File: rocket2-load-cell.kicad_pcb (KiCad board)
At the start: 2 copper layers, 69 x 67 mm, 38 parts, among them J1 SWD, J2 Screw_Terminal_01x02, U2 STM32F103C8Tx, U3 AMS1117-3.3, Y1 16MHz

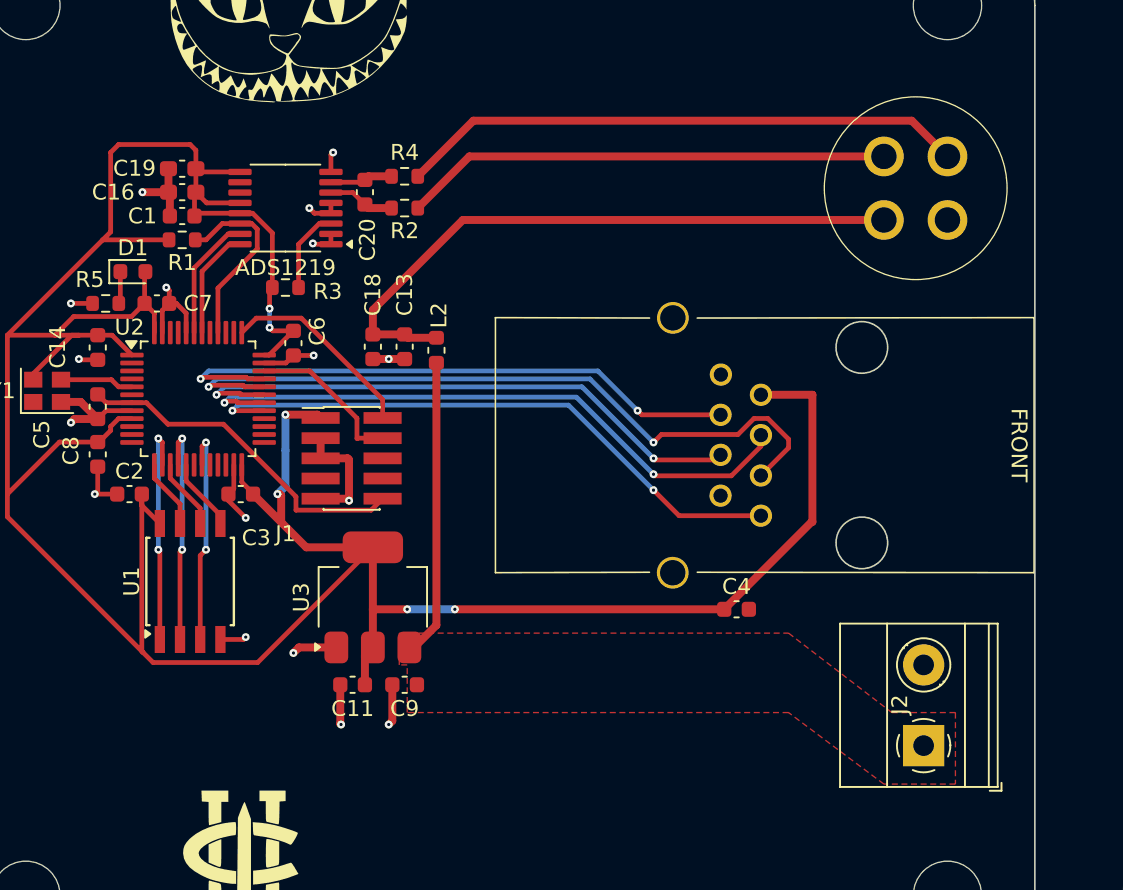
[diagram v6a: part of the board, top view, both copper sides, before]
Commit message: added gx12 connector and fixed varioius other design problems
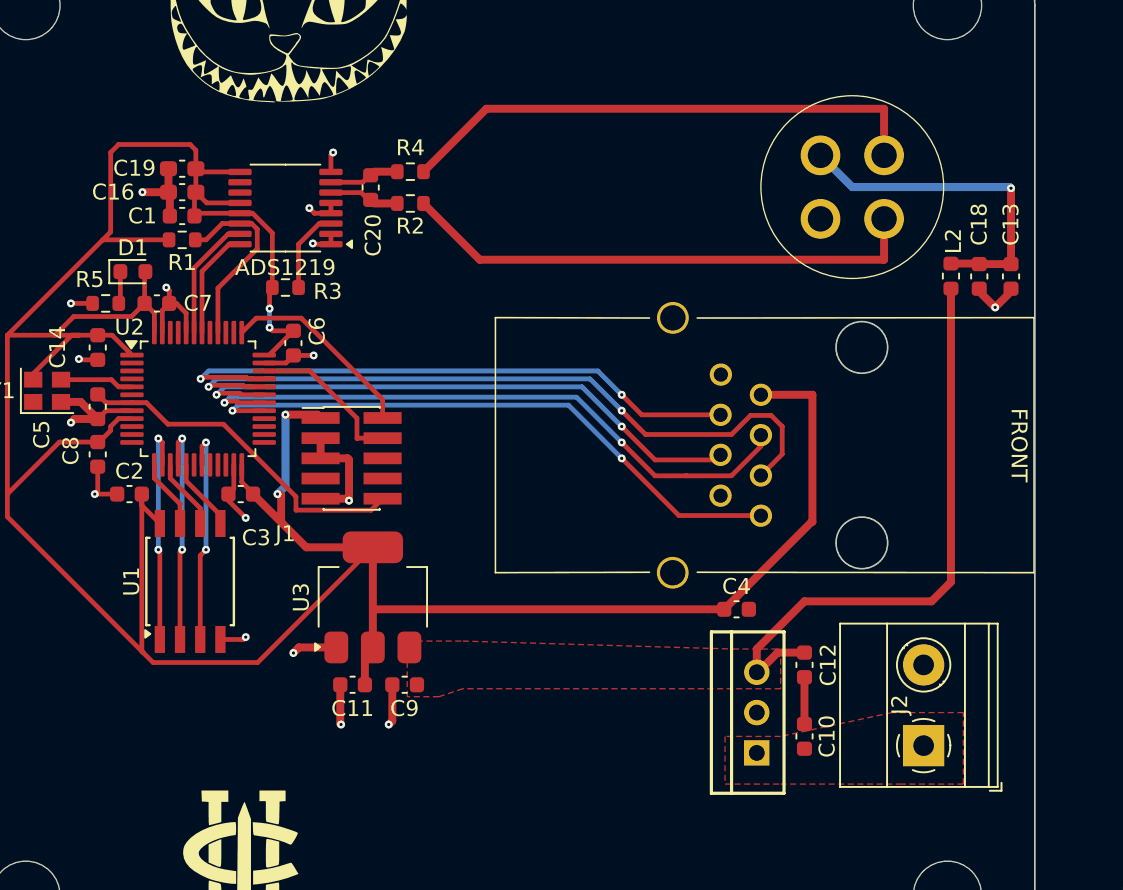
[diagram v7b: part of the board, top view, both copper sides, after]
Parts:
- added C10: .33uF, Capacitor_SMD:C_0603_1608Metric, F.Cu at (175.0, 133.5)
- added C12: .1uF, Capacitor_SMD:C_0603_1608Metric, F.Cu at (175.0, 129.0)
- added U4: UA7812CKCS, ucirp:KCS0003B, F.Cu at (172.0, 132.0)
- moved C13 38.4 mm to (188.0, 104.5)
- moved C18 38.4 mm to (186.0, 104.5)
- moved L2 32.7 mm to (184.2, 104.5)
- moved GX12 3.99 mm to (178.0, 98.9)
- moved C20 0.46 mm to (147.7, 99.0)
- moved R2 0.46 mm to (150.2, 100.0)
- moved R4 0.46 mm to (150.2, 98.0)
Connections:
- C13 pad 1: Net-(C13-Pad1) -> VLC
- C18 pad 1: Net-(C13-Pad1) -> VLC
- GX12 pad 1: AIN+ -> AIN-
- GX12 pad 2: GND -> VLC
- GX12 pad 3: Net-(C13-Pad1) -> GND
- GX12 pad 4: AIN- -> AIN+
- J2 pad 1: VBUS -> VIN
- L2 pad 1: Net-(C13-Pad1) -> VLC
- R2 pad 1: AIN- -> AIN+
- R4 pad 1: AIN+ -> AIN-
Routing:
- net Net-(C13-Pad1): track 40.1 -> 0.00 mm
- net VLC: track 0.00 -> 21.4 mm, vias 0 -> 1
- net VBUS: track 18.8 -> 37.4 mm
- net GND: track 54.6 -> 58.2 mm
- net AIN-: track 30.7 -> 33.5 mm
- net AIN+: track 35.7 -> 33.0 mm
- net +3.3V: track 207.0 -> 204.9 mm, vias 6 -> 4
- net MEM_MOSI: track 4.58 -> 4.06 mm
- added copper zone on F.Cu, net VIN

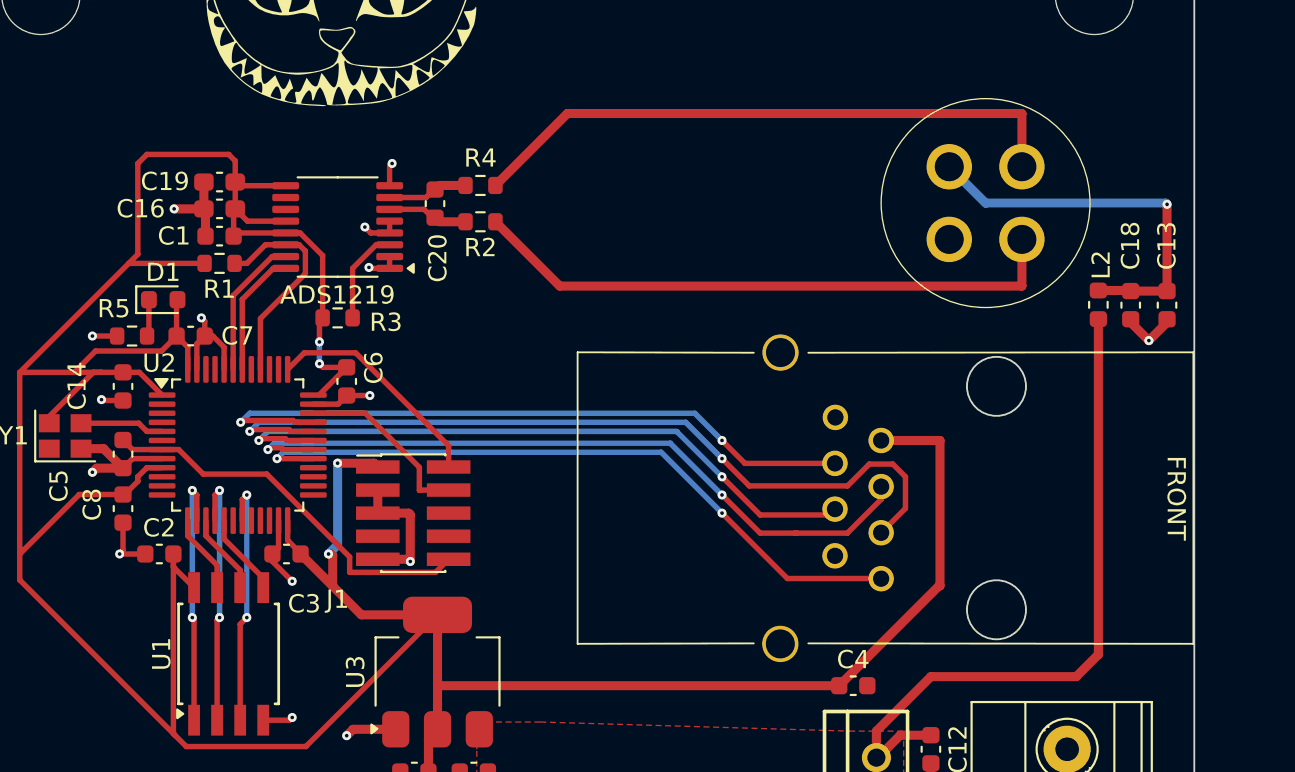
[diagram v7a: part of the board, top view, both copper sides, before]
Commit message: changed via locations
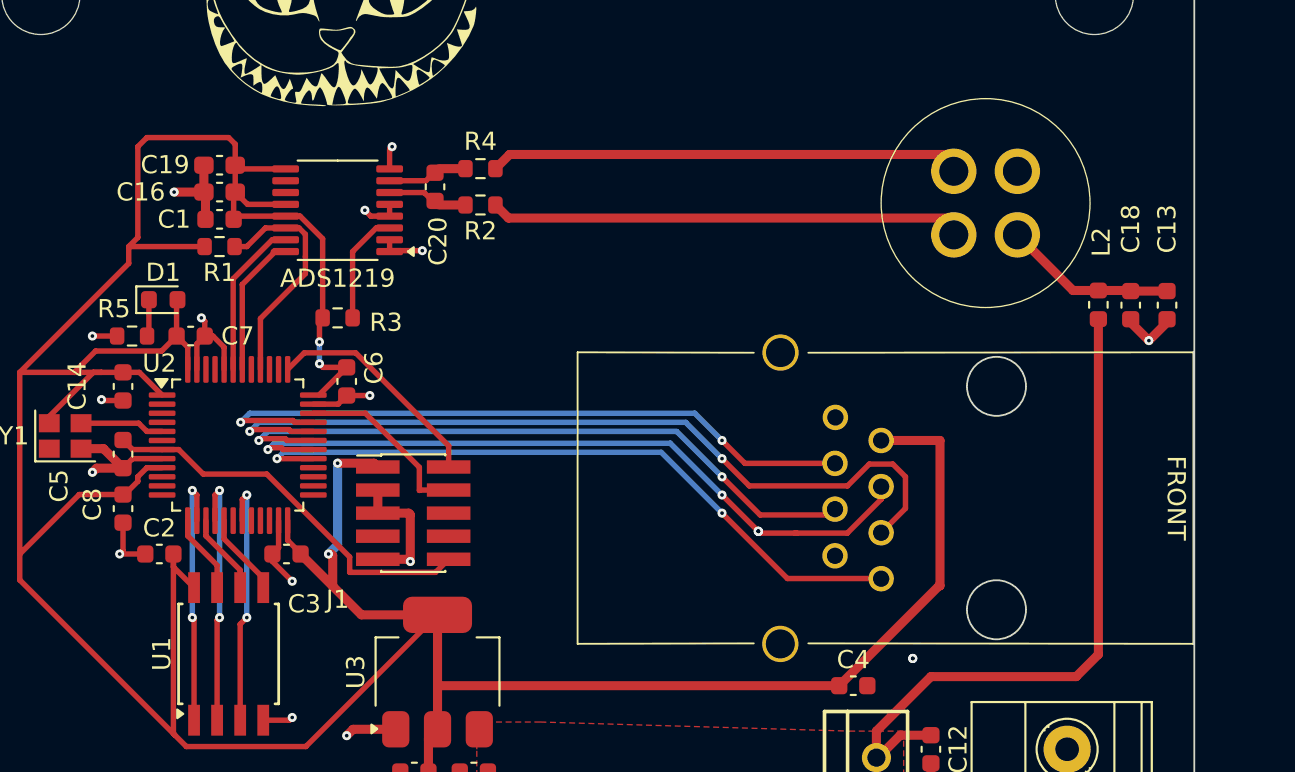
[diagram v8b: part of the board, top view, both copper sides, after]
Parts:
- moved ADS1219 0.92 mm to (142.3, 99.3)
- moved C1 0.92 mm to (135.8, 99.8)
- moved C16 0.92 mm to (135.8, 98.3)
- moved C19 0.92 mm to (135.8, 96.8)
- moved C20 0.92 mm to (147.7, 98.0)
- moved R1 0.92 mm to (135.8, 101.3)
- moved R2 0.92 mm to (150.2, 99.0)
- moved R4 0.92 mm to (150.2, 97.0)
- turned GX12 to 180 degrees
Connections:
- R2 pad 1: AIN+ -> AIN-
- R4 pad 1: AIN- -> AIN+
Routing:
- net VLC: track 21.4 -> 9.48 mm, vias 1 -> 0
- net AIN-: track 33.5 -> 25.5 mm
- net AIN+: track 33.0 -> 25.6 mm
- net +3.3V: track 204.9 -> 206.7 mm
- net ADS_CLK: track 6.95 -> 8.49 mm
- net ADS_DATA: track 7.84 -> 8.77 mm
- net Net-(ADS1219-RESET): track 5.30 -> 6.23 mm
- net ADS_DRDY: track 12.0 -> 12.9 mm
- net GND: track 58.2 -> 58.9 mm, vias 17 -> 19
- net ETH_TX: vias 2 -> 5
